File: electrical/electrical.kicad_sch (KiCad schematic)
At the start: 0 parts

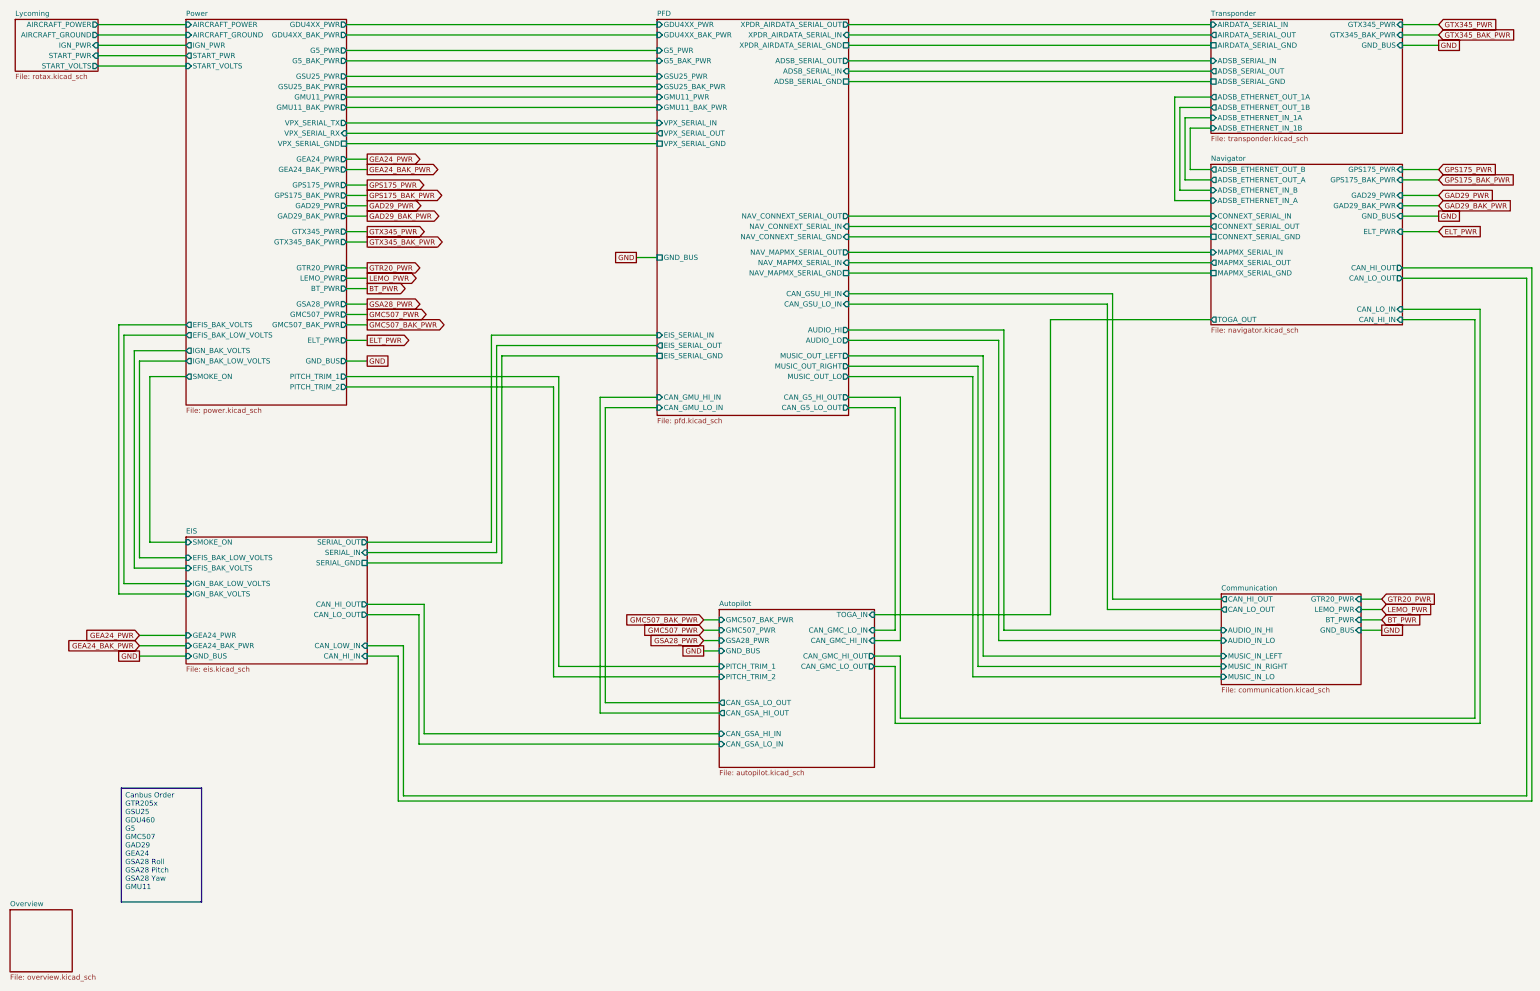
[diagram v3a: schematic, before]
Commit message: Added connectors and non-CAN/RS232/Ethernet shields.
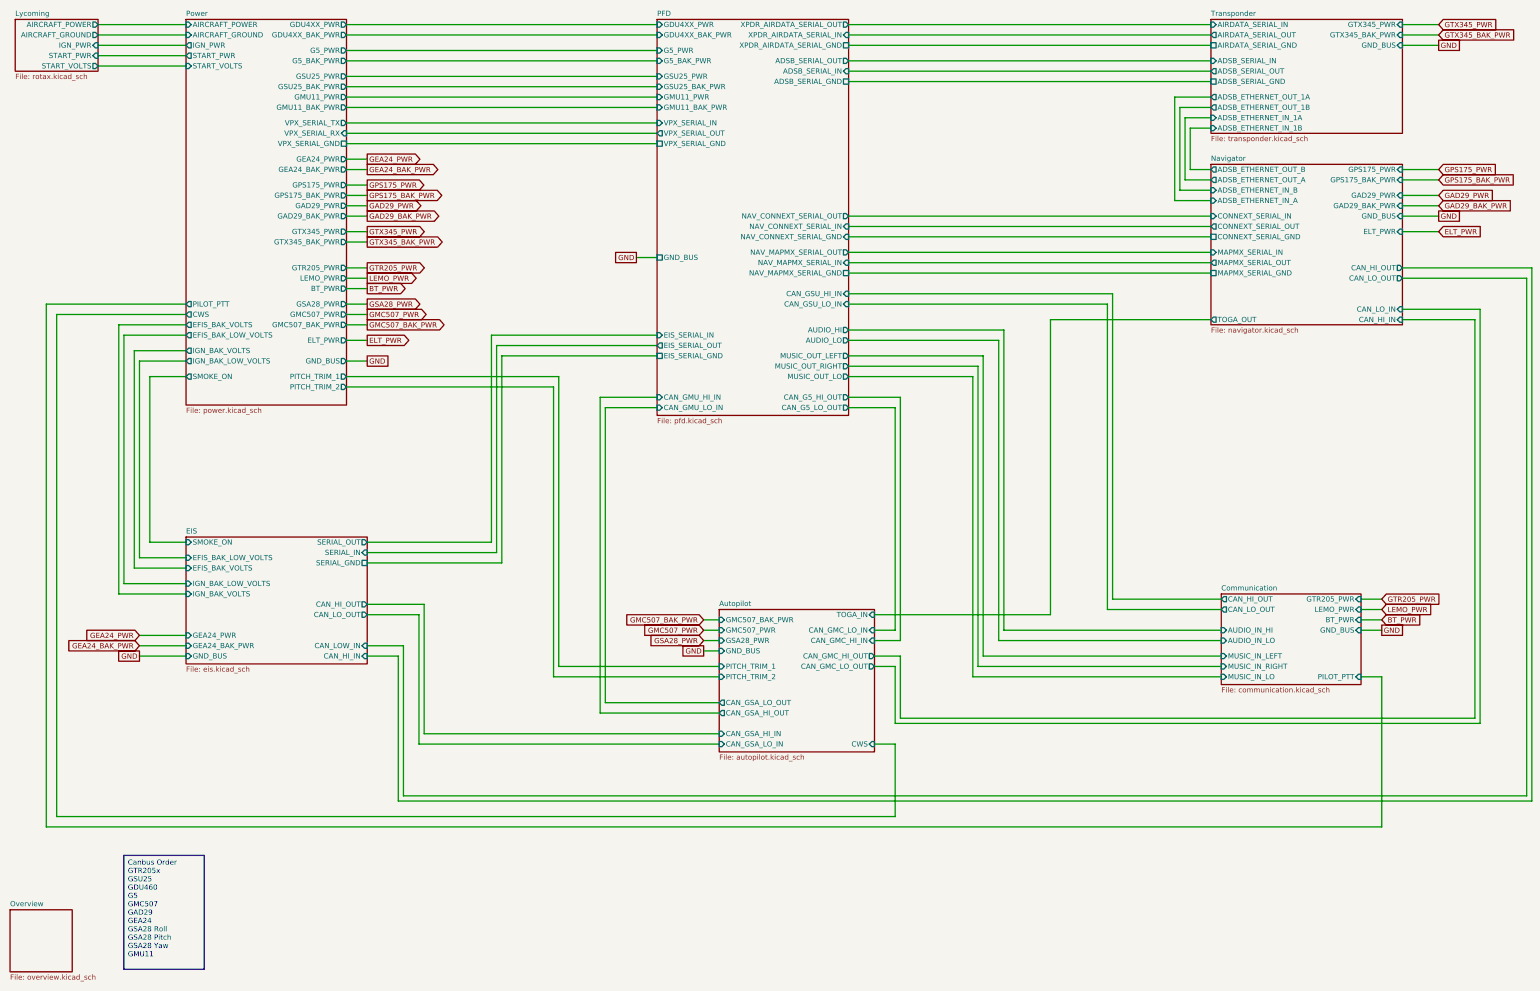
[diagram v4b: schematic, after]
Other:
- sheet Autopilot ports: added CWS; removed none
- sheet Communication ports: added GTR205_PWR, PILOT_PTT; removed GTR20_PWR
- sheet Power ports: added CWS, GTR205_PWR, PILOT_PTT; removed GTR20_PWR
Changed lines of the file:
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@@
 	(title_block
 		(title "Electrical Overview")
-		(date "2025-09-29")
-		(rev "1.0.7")
+		(date "2025-10-01")
+		(rev "1.1")
 		(company "N78HR")
 	)
 	(text_box "Canbus Order\nGTR205x\nGSU25\nGDU460\nG5\nGMC507\nGAD29\nGEA24\nGSA28 Roll\nGSA28 Pitch\nGSA28 Yaw\nGMU11"
 		(exclude_from_sim no)
-		(at 42.545 217.805 0)
+		(at 43.18 234.315 0)
 		(size 19.685 27.94)
 		(margins 0.9525 0.9525 0.9525 0.9525)
@@
 	(wire
 		(pts
+			(xy 232.41 224.79) (xy 232.41 207.01)
+		)
+		(stroke
+			(width 0)
+			(type default)
+		)
+	)
+	(wire
+		(pts
 			(xy 97.79 107.95) (xy 102.87 107.95)
 		)
@@
 	(wire
 		(pts
+			(xy 351.79 227.33) (xy 351.79 190.5)
+		)
+		(stroke
+			(width 0)
+			(type default)
+		)
+	)
+	(wire
+		(pts
+			(xy 232.41 207.01) (xy 227.33 207.01)
+		)
+		(stroke
+			(width 0)
+			(type default)
+		)
+	)
+	(wire
+		(pts
 			(xy 46.99 113.03) (xy 46.99 161.29)
 		)
@@
 	(wire
 		(pts
+			(xy 24.13 99.06) (xy 24.13 227.33)
+		)
+		(stroke
+			(width 0)
+			(type default)
+		)
+	)
+	(wire
+		(pts
 			(xy 254 111.76) (xy 254 185.42)
 		)
@@
 	(wire
 		(pts
+			(xy 58.42 101.6) (xy 26.67 101.6)
+		)
+		(stroke
+			(width 0)
+			(type default)
+		)
+	)
+	(wire
+		(pts
 			(xy 97.79 116.84) (xy 149.86 116.84)
 		)
@@
 	(wire
 		(pts
+			(xy 26.67 101.6) (xy 26.67 224.79)
+		)
+		(stroke
+			(width 0)
+			(type default)
+		)
+	)
+	(wire
+		(pts
 			(xy 97.79 90.17) (xy 102.87 90.17)
 		)
@@
 	(wire
 		(pts
+			(xy 26.67 224.79) (xy 232.41 224.79)
+		)
+		(stroke
+			(width 0)
+			(type default)
+		)
+	)
+	(wire
+		(pts
 			(xy 356.87 68.58) (xy 365.76 68.58)
 		)
@@
 	(wire
 		(pts
+			(xy 24.13 227.33) (xy 351.79 227.33)
+		)
+		(stroke
+			(width 0)
+			(type default)
+		)
+	)
+	(wire
+		(pts
+			(xy 351.79 190.5) (xy 346.71 190.5)
+		)
+		(stroke
+			(width 0)
+			(type default)
+		)
+	)
+	(wire
+		(pts
 			(xy 284.48 99.06) (xy 284.48 173.99)
 		)
@@
 	(wire
 		(pts
+			(xy 58.42 99.06) (xy 24.13 99.06)
+		)
+		(stroke
+			(width 0)
+			(type default)
+		)
+	)
+	(wire
+		(pts
 			(xy 220.98 116.84) (xy 251.46 116.84)
 		)
@@
 		)
 	)
-	(global_label "GTR20_PWR"
+	(global_label "GTR205_PWR"
 		(shape output)
 		(at 102.87 90.17 0)
@@
 		)
 		(property "Intersheetrefs" "${INTERSHEET_REFS}"
-			(at 116.7408 90.17 0)
+			(at 117.9503 90.17 0)
 			(effects
 				(font
@@
 		)
 	)
-	(global_label "GTR20_PWR"
+	(global_label "GTR205_PWR"
 		(shape input)
 		(at 351.79 171.45 0)
@@
 		)
 		(property "Intersheetrefs" "${INTERSHEET_REFS}"
-			(at 365.6608 171.45 0)
+			(at 366.8703 171.45 0)
 			(effects
 				(font
@@
 			)
 		)
-		(pin "GTR20_PWR" output
+		(pin "GTR205_PWR" output
 			(at 97.79 90.17 0)
 			(effects
@@
 			)
 		)
+		(pin "CWS" output
+			(at 58.42 101.6 180)
+			(effects
+				(font
+					(size 1.27 1.27)
+				)
+				(justify left)
+			)
+		)
+		(pin "PILOT_PTT" output
+			(at 58.42 99.06 180)
+			(effects
+				(font
+					(size 1.27 1.27)
+				)
+				(justify left)
+			)
+		)
 		(instances
 			(project "electrical"
@@
 	(sheet
 		(at 189.23 173.99)
-		(size 38.1 38.735)
+		(size 38.1 34.925)
 		(exclude_from_sim no)
 		(in_bom yes)
@@
 		)
 		(property "Sheetfile" "autopilot.kicad_sch"
-			(at 189.23 213.3096 0)
+			(at 189.23 209.4996 0)
 			(effects
 				(font
@@
 			)
 		)
+		(pin "CWS" input
+			(at 227.33 207.01 0)
+			(effects
+				(font
+					(size 1.27 1.27)
+				)
+				(justify right)
+			)
+		)
 		(instances
 			(project "electrical"
@@
 			)
 		)
-		(pin "GTR20_PWR" input
+		(pin "GTR205_PWR" input
 			(at 346.71 171.45 0)
 			(effects
@@
 			(effects
 				(font
+					(size 1.27 1.27)
+				)
+				(justify right)
+			)
+		)
+		(pin "PILOT_PTT" input
+			(at 346.71 190.5 0)
+			(effects
+				(font
